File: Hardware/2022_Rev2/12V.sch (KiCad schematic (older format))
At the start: 0 parts

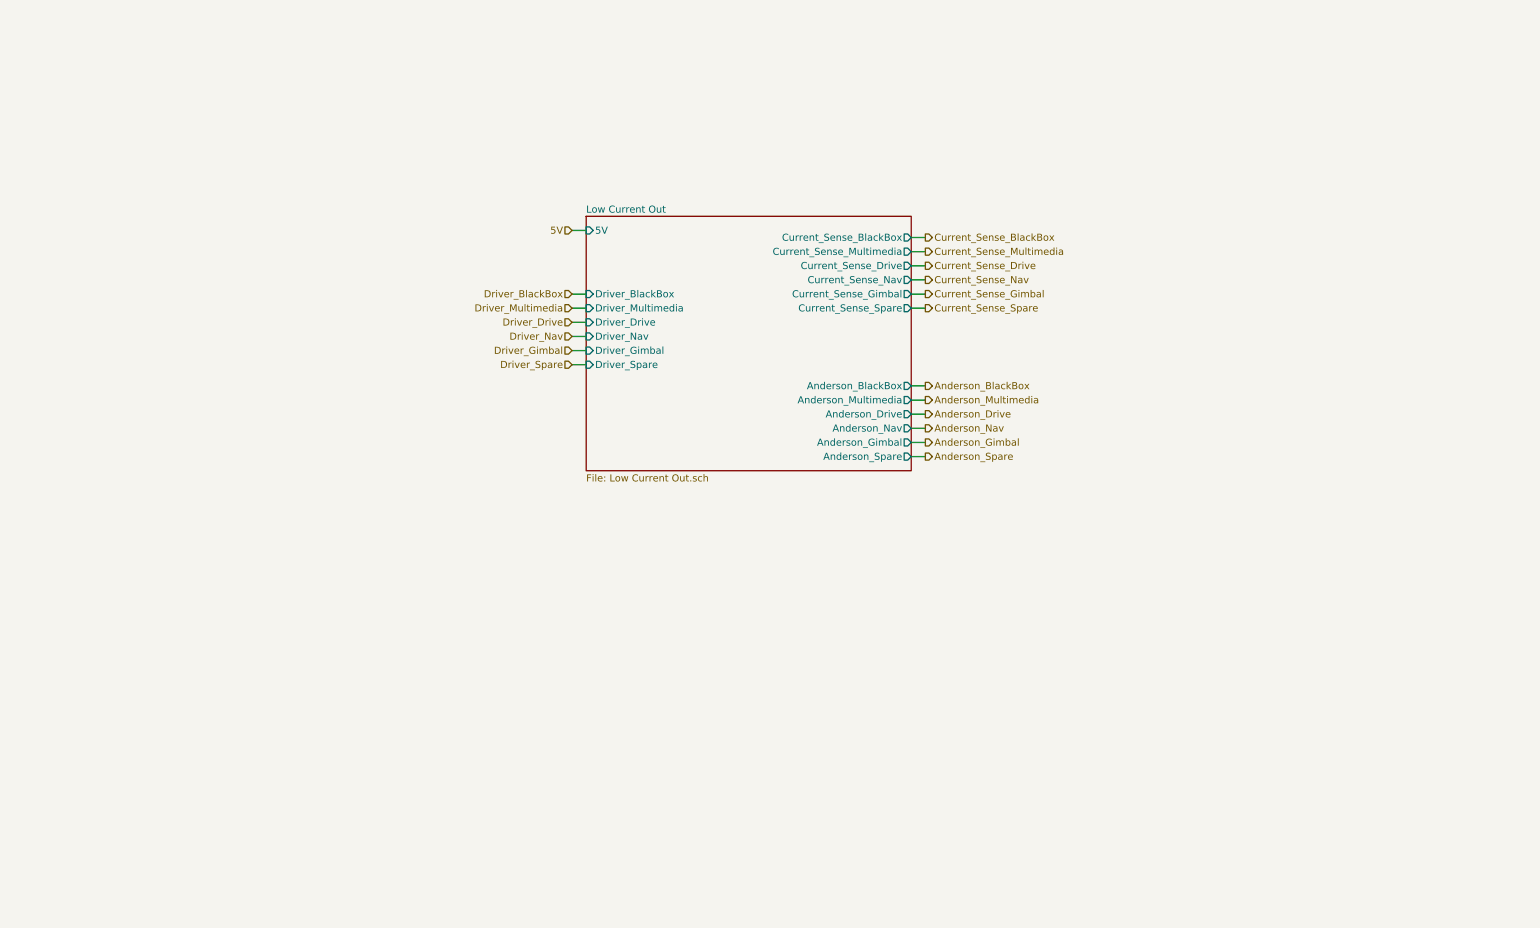
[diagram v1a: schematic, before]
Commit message: change switch circuit naming + added more switch circuits.
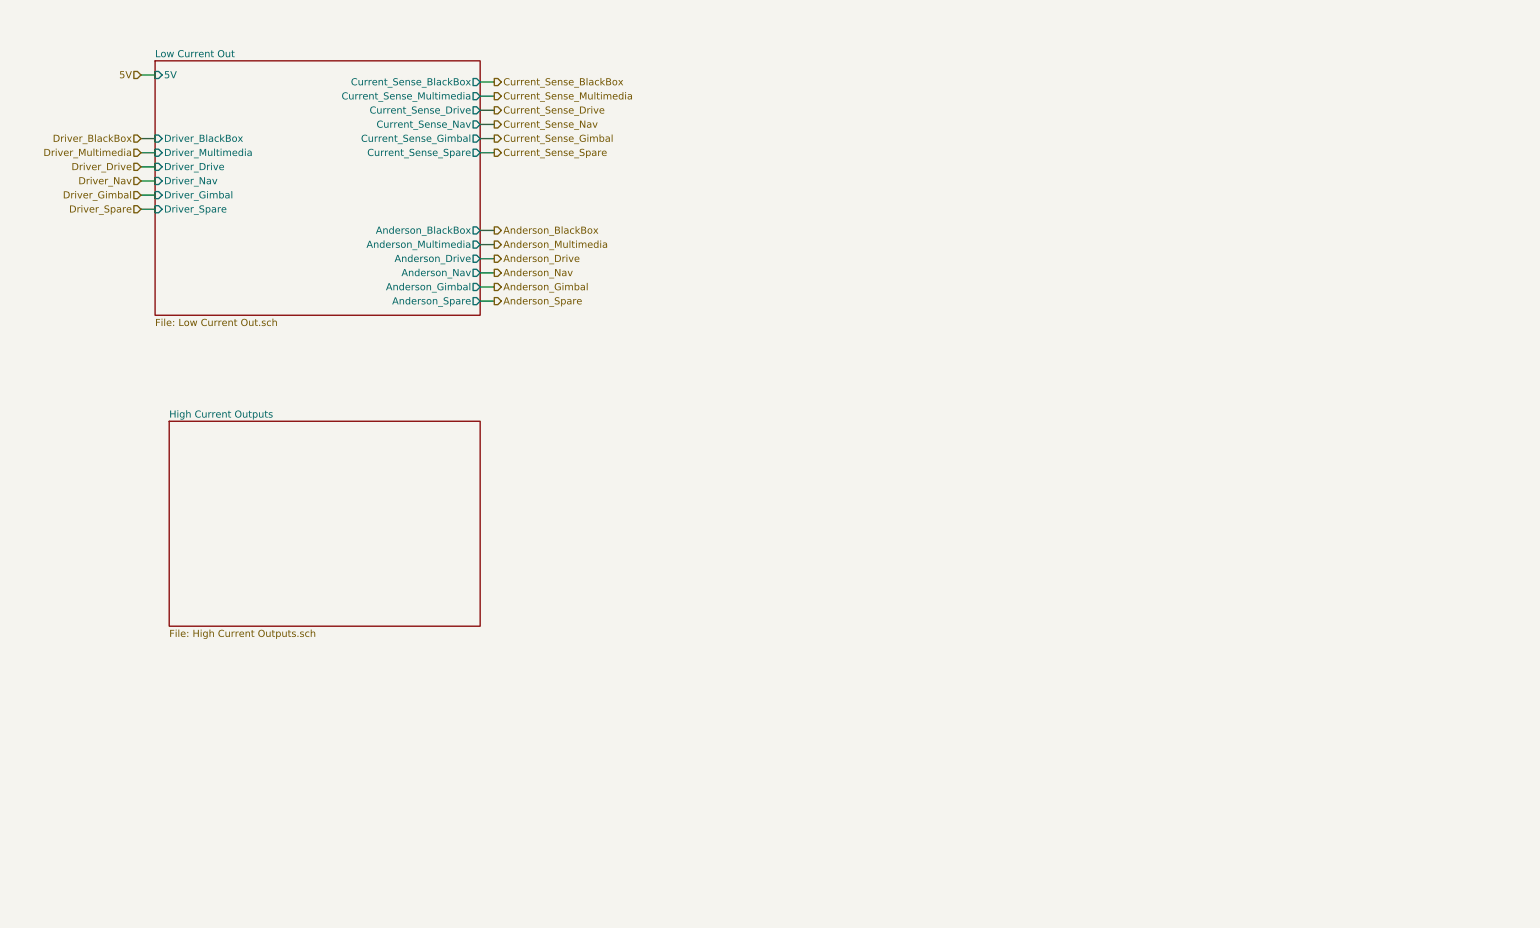
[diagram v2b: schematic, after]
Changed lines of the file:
@@
 $EndDescr
 $Sheet
-S 4500 2000 2300 1800
+S 1450 900  2300 1800
 U 621219B0
 F0 "Low Current Out" 50
 F1 "Low Current Out.sch" 50
-F2 "Current_Sense_BlackBox" O R 6800 2150 50
-F3 "Anderson_BlackBox" O R 6800 3200 50
-F4 "Driver_BlackBox" I L 4500 2550 50
-F5 "5V" I L 4500 2100 50
-F6 "Current_Sense_Multimedia" O R 6800 2250 50
-F7 "Anderson_Multimedia" O R 6800 3300 50
-F8 "Driver_Multimedia" I L 4500 2650 50
-F9 "Current_Sense_Drive" O R 6800 2350 50
-F10 "Anderson_Drive" O R 6800 3400 50
-F11 "Driver_Drive" I L 4500 2750 50
-F12 "Current_Sense_Nav" O R 6800 2450 50
-F13 "Anderson_Nav" O R 6800 3500 50
-F14 "Driver_Nav" I L 4500 2850 50
-F15 "Current_Sense_Gimbal" O R 6800 2550 50
-F16 "Anderson_Gimbal" O R 6800 3600 50
-F17 "Driver_Gimbal" I L 4500 2950 50
-F18 "Current_Sense_Spare" O R 6800 2650 50
-F19 "Anderson_Spare" O R 6800 3700 50
-F20 "Driver_Spare" I L 4500 3050 50
+F2 "Current_Sense_BlackBox" O R 3750 1050 50
+F3 "Anderson_BlackBox" O R 3750 2100 50
+F4 "Driver_BlackBox" I L 1450 1450 50
+F5 "5V" I L 1450 1000 50
+F6 "Current_Sense_Multimedia" O R 3750 1150 50
+F7 "Anderson_Multimedia" O R 3750 2200 50
+F8 "Driver_Multimedia" I L 1450 1550 50
+F9 "Current_Sense_Drive" O R 3750 1250 50
+F10 "Anderson_Drive" O R 3750 2300 50
+F11 "Driver_Drive" I L 1450 1650 50
+F12 "Current_Sense_Nav" O R 3750 1350 50
+F13 "Anderson_Nav" O R 3750 2400 50
+F14 "Driver_Nav" I L 1450 1750 50
+F15 "Current_Sense_Gimbal" O R 3750 1450 50
+F16 "Anderson_Gimbal" O R 3750 2500 50
+F17 "Driver_Gimbal" I L 1450 1850 50
+F18 "Current_Sense_Spare" O R 3750 1550 50
+F19 "Anderson_Spare" O R 3750 2600 50
+F20 "Driver_Spare" I L 1450 1950 50
 $EndSheet
-Text HLabel 4400 2100 0    50   Input ~ 0
+Text HLabel 1350 1000 0    50   Input ~ 0
 5V
-Text HLabel 4400 2550 0    50   Input ~ 0
+Text HLabel 1350 1450 0    50   Input ~ 0
 Driver_BlackBox
-Text HLabel 4400 2650 0    50   Input ~ 0
+Text HLabel 1350 1550 0    50   Input ~ 0
 Driver_Multimedia
-Text HLabel 4400 2750 0    50   Input ~ 0
+Text HLabel 1350 1650 0    50   Input ~ 0
 Driver_Drive
-Text HLabel 4400 2850 0    50   Input ~ 0
+Text HLabel 1350 1750 0    50   Input ~ 0
 Driver_Nav
-Text HLabel 4400 2950 0    50   Input ~ 0
+Text HLabel 1350 1850 0    50   Input ~ 0
 Driver_Gimbal
-Text HLabel 4400 3050 0    50   Input ~ 0
+Text HLabel 1350 1950 0    50   Input ~ 0
 Driver_Spare
 Wire Wire Line
-	4400 2100 4500 2100
+	1350 1000 1450 1000
 Wire Wire Line
-	4400 2550 4500 2550
+	1350 1450 1450 1450
 Wire Wire Line
-	4500 2650 4400 2650
+	1450 1550 1350 1550
 Wire Wire Line
-	4400 2750 4500 2750
+	1350 1650 1450 1650
 Wire Wire Line
-	4500 2850 4400 2850
+	1450 1750 1350 1750
 Wire Wire Line
-	4400 2950 4500 2950
+	1350 1850 1450 1850
 Wire Wire Line
-	4500 3050 4400 3050
-Text HLabel 6900 2150 2    50   Output ~ 0
+	1450 1950 1350 1950
+Text HLabel 3850 1050 2    50   Output ~ 0
 Current_Sense_BlackBox
-Text HLabel 6900 2250 2    50   Output ~ 0
+Text HLabel 3850 1150 2    50   Output ~ 0
 Current_Sense_Multimedia
-Text HLabel 6900 2350 2    50   Output ~ 0
+Text HLabel 3850 1250 2    50   Output ~ 0
 Current_Sense_Drive
-Text HLabel 6900 2450 2    50   Output ~ 0
+Text HLabel 3850 1350 2    50   Output ~ 0
 Current_Sense_Nav
-Text HLabel 6900 2550 2    50   Output ~ 0
+Text HLabel 3850 1450 2    50   Output ~ 0
 Current_Sense_Gimbal
-Text HLabel 6900 2650 2    50   Output ~ 0
+Text HLabel 3850 1550 2    50   Output ~ 0
 Current_Sense_Spare
 Wire Wire Line
-	6900 2650 6800 2650
+	3850 1550 3750 1550
 Wire Wire Line
-	6800 2550 6900 2550
+	3750 1450 3850 1450
 Wire Wire Line
-	6900 2450 6800 2450
+	3850 1350 3750 1350
 Wire Wire Line
-	6800 2350 6900 2350
+	3750 1250 3850 1250
 Wire Wire Line
-	6900 2250 6800 2250
+	3850 1150 3750 1150
 Wire Wire Line
-	6800 2150 6900 2150
-Text HLabel 6900 3200 2    50   Output ~ 0
+	3750 1050 3850 1050
+Text HLabel 3850 2100 2    50   Output ~ 0
 Anderson_BlackBox
-Text HLabel 6900 3300 2    50   Output ~ 0
+Text HLabel 3850 2200 2    50   Output ~ 0
 Anderson_Multimedia
-Text HLabel 6900 3400 2    50   Output ~ 0
+Text HLabel 3850 2300 2    50   Output ~ 0
 Anderson_Drive
-Text HLabel 6900 3500 2    50   Output ~ 0
+Text HLabel 3850 2400 2    50   Output ~ 0
 Anderson_Nav
-Text HLabel 6900 3600 2    50   Output ~ 0
+Text HLabel 3850 2500 2    50   Output ~ 0
 Anderson_Gimbal
-Text HLabel 6900 3700 2    50   Output ~ 0
+Text HLabel 3850 2600 2    50   Output ~ 0
 Anderson_Spare
 Wire Wire Line
-	6900 3200 6800 3200
+	3850 2100 3750 2100
 Wire Wire Line
-	6800 3300 6900 3300
+	3750 2200 3850 2200
 Wire Wire Line
-	6900 3400 6800 3400
+	3850 2300 3750 2300
 Wire Wire Line
-	6800 3500 6900 3500
+	3750 2400 3850 2400
 Wire Wire Line
-	6900 3600 6800 3600
+	3850 2500 3750 2500
 Wire Wire Line
-	6800 3700 6900 3700
+	3750 2600 3850 2600
+$Sheet
+S 1550 3450 2200 1450
+U 622EFCD1
+F0 "High Current Outputs" 50
+F1 "High Current Outputs.sch" 50
+$EndSheet
 $EndSCHEMATC

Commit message: back to the teensy :alien:
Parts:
- added C? (x2): 0.1uF, symbol Device:C
- added C? (x2): 10uF, symbol Device:C
- added D? (x2): LED, symbol Device:D
- added Q? (x2): BUK768R3-60E, Package_TO_SOT_SMD:LFPAK33, symbol Transistor_FET:BUK7M9R9-60EX
- added R? (x2): 5.1k, symbol Device:R
- added R? (x2): 330, symbol Device:R
- added R? (x2): 0.0025, symbol Device:R
- added U? (x2): LT1910, symbol 2022_Rev2-rescue:LT1910-MRDT_ICs
- added U? (x2): INA281, Package_TO_SOT_SMD:SOT-23-5, symbol 2022_Rev2-rescue:INA281-MRDT_ICs
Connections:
- net 5V: now also R?.1, R?.1, U?.5 (V+), U?.5 (V+)
- net Anderson_Drive: now also R?.2, R?.2, U?.4 (-), U?.4 (-)
- net Current_Sense_Drive: now also U?.1, U?.1
- net Driver_Drive: now also U?.4 (IN), U?.4 (IN)
- new net: R?.2, U?.3 (FAULT) (x2)
- new net: C?.1, U?.2 (TIMER) (x2)
- new net: Q?.4 (G), U?.5 (GATE) (x2)
- new net: C?.1, Q?.5 (D), U?.6 (SENSE), U?.8 (V+) (x2)
- new net: Q?.1 (S), Q?.2 (S), Q?.3 (S), R?.1, R?.2, U?.3 (+) (x2)
- new net: D?.2 (A), R?.1 (x2)
- new net GND: C?.2, C?.2, C?.2, C?.2, D?.1 (K), D?.1 (K), U?.1 (GND), U?.1 (GND), U?.2 (GND), U?.2 (GND)
